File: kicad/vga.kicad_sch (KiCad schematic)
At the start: 31 parts, among them J2 DE15_Receptacle_HighDensity_M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, Q2 BC547, U17 74HC174, U18 XC9536PC44, U19 74HC244, U20 74HC574, U21 74HC245, U22 74HC02, U24 6264, U25 74HC574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

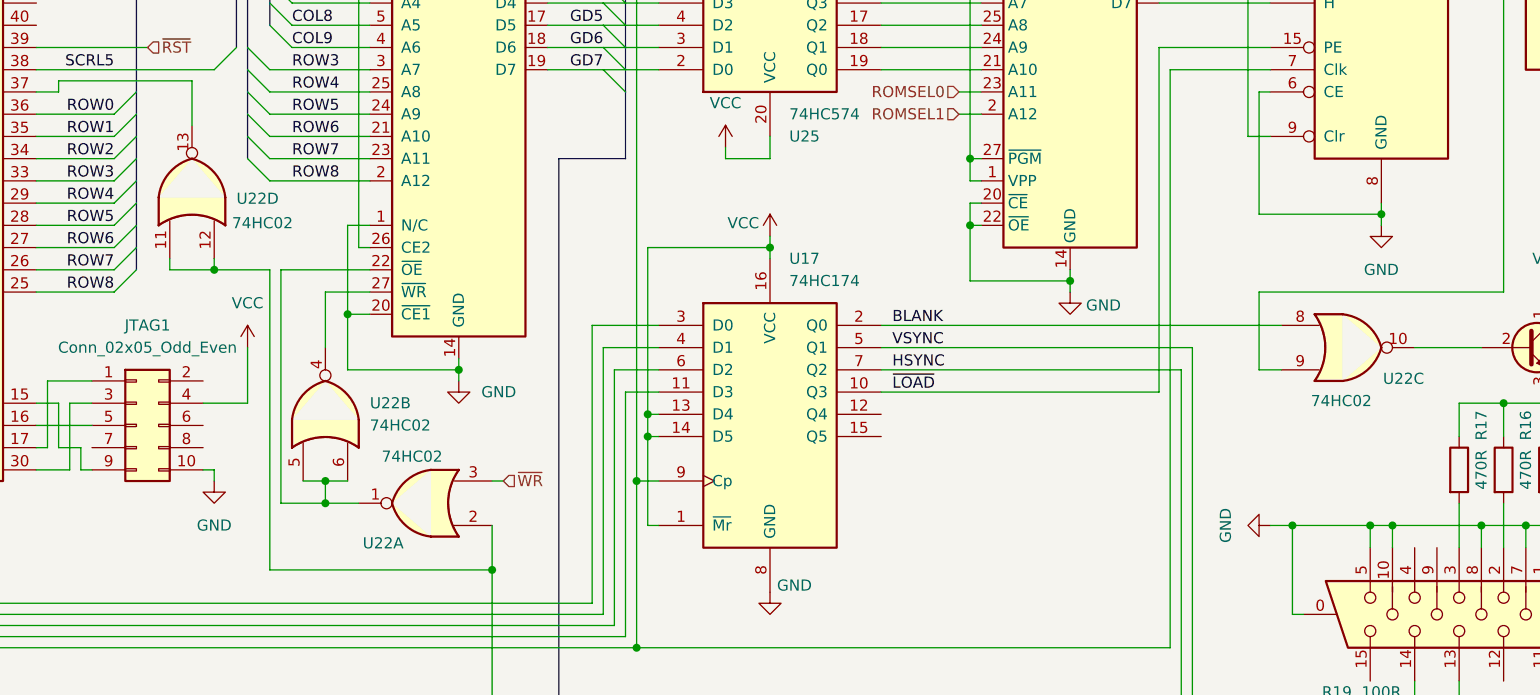
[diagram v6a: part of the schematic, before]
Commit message: hw: rev D - replace DB25 connector footprint with available one
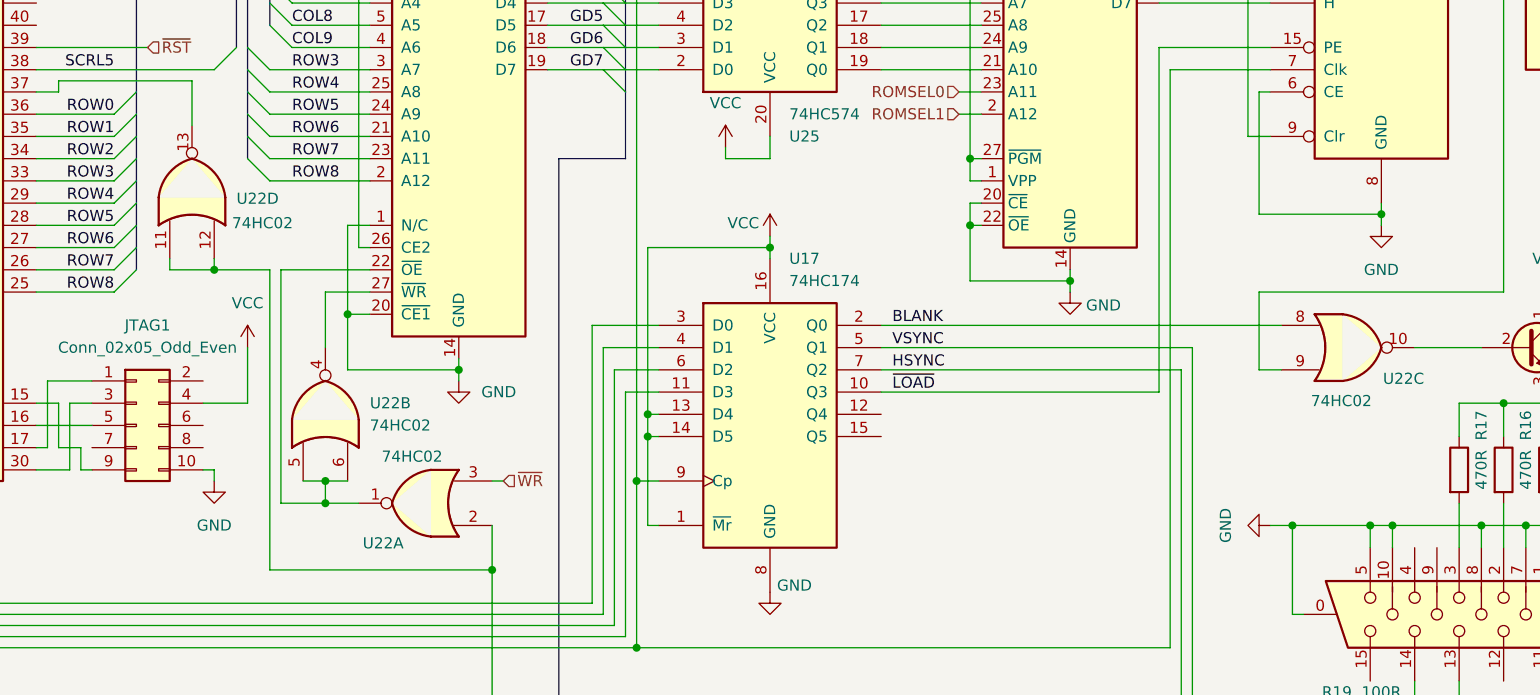
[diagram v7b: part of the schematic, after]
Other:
- company: (none) -> A.K.
- title: (none) -> VGA
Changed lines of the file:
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@@
 (kicad_sch
-	(version 20231120)
+	(version 20250114)
 	(generator "eeschema")
-	(generator_version "8.0")
+	(generator_version "9.0")
 	(paper "A3")
+	(title_block
+		(title "VGA")
+		(date "2025-08-04")
+		(rev "D")
+		(company "A.K.")
+	)
 	(junction
 		(at 227.33 201.93)
